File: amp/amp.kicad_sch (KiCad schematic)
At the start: 79 parts, among them J1 HI Input, J2 Speaker 8Ω, J3 Headphones, J4 LO Input, J6 FX Send, J7 FX Return, Q1 S8050, SW1 PWR, SW2 FX Enable/Bypass, U1 TL074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

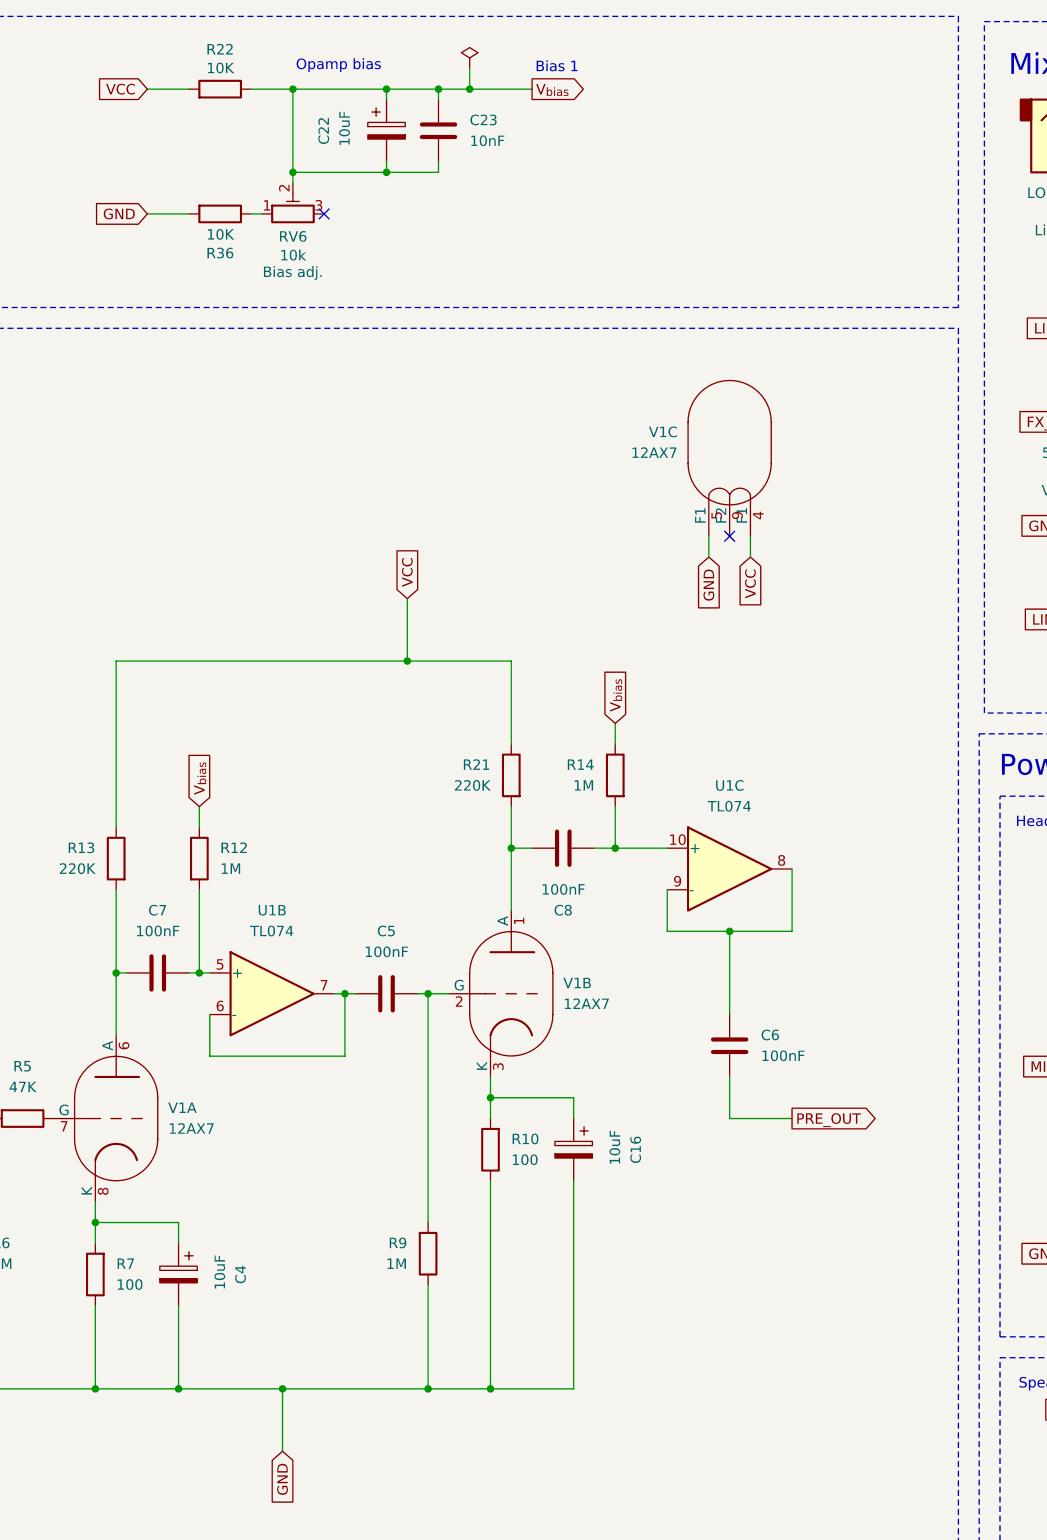
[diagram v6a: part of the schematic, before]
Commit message: Simplify opamp bias source
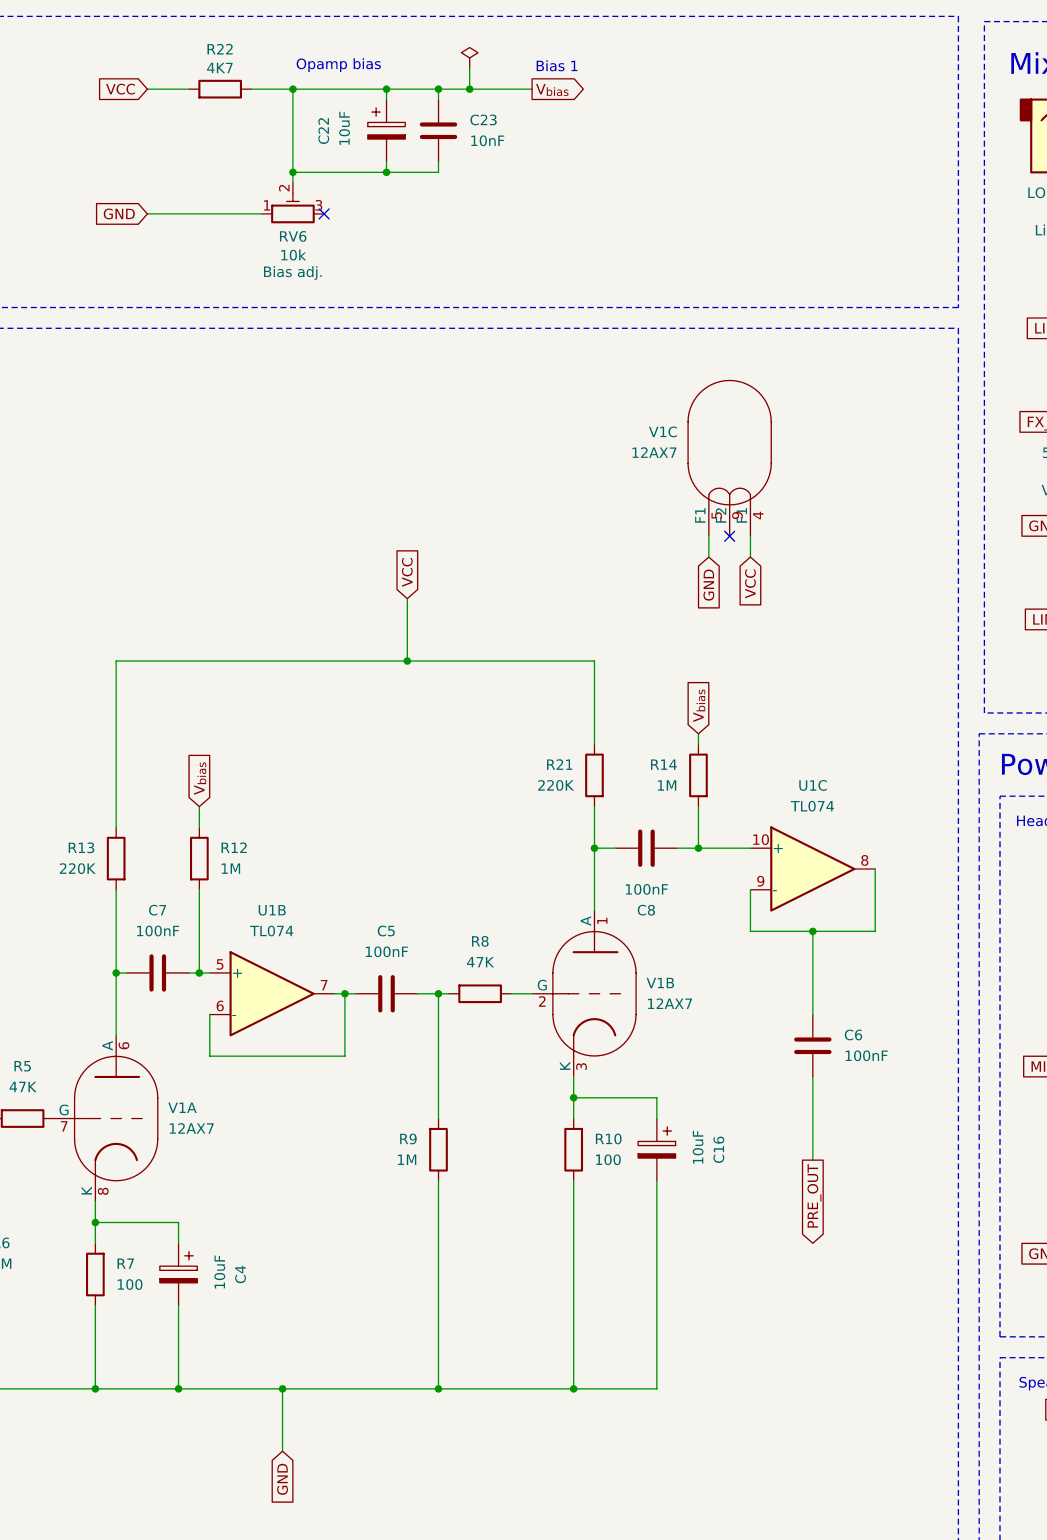
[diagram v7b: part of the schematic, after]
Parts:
- removed R36: 10K, symbol Device:R
- added R8: 47K, symbol Device:R
- R22: value 10K -> 4K7
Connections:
- net GND: now also RV6.1
- net at C5.2, R9.2: now also R8.2; no longer V1.2 (G)
- new net: R8.1, V1.2 (G)
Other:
- moved on the sheet: C16, C6, C8, R10, R14, R21, R9, U1C, V1B

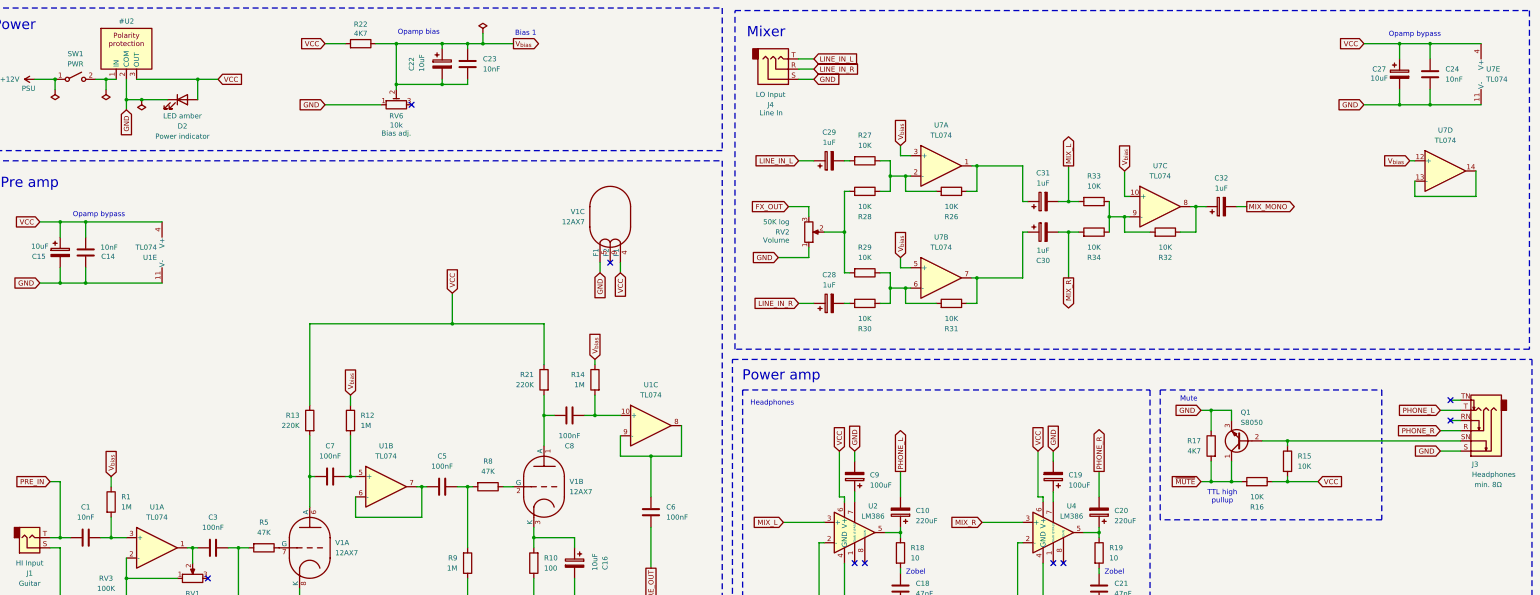
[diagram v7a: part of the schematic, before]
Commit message: Pulldown mix opamp inputs to gnd
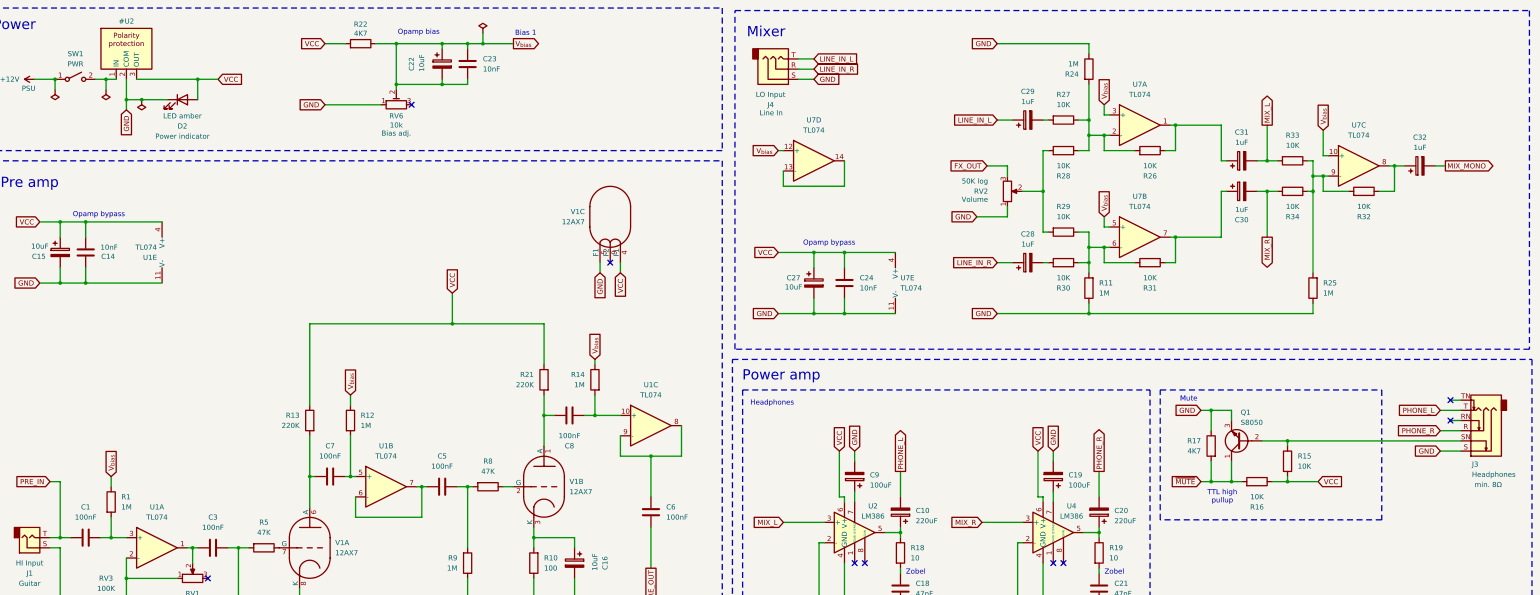
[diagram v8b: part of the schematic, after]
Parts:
- added R11, R24, R25: 1M, symbol Device:R
- C1: value 10nF -> 100nF
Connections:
- net GND: now also R11.1, R24.1, R25.1
- net at R32.2, R33.1, R34.1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: now also R25.2
- net at R29.1, R30.1, R31.2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: now also R11.2
- net at R26.2, R27.1, R28.1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: now also R24.2
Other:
- moved on the sheet: C24, C27, C28, C29, C30, C31, C32, R26, R27, R28, R29, R30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
